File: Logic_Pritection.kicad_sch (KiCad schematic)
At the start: 18 parts

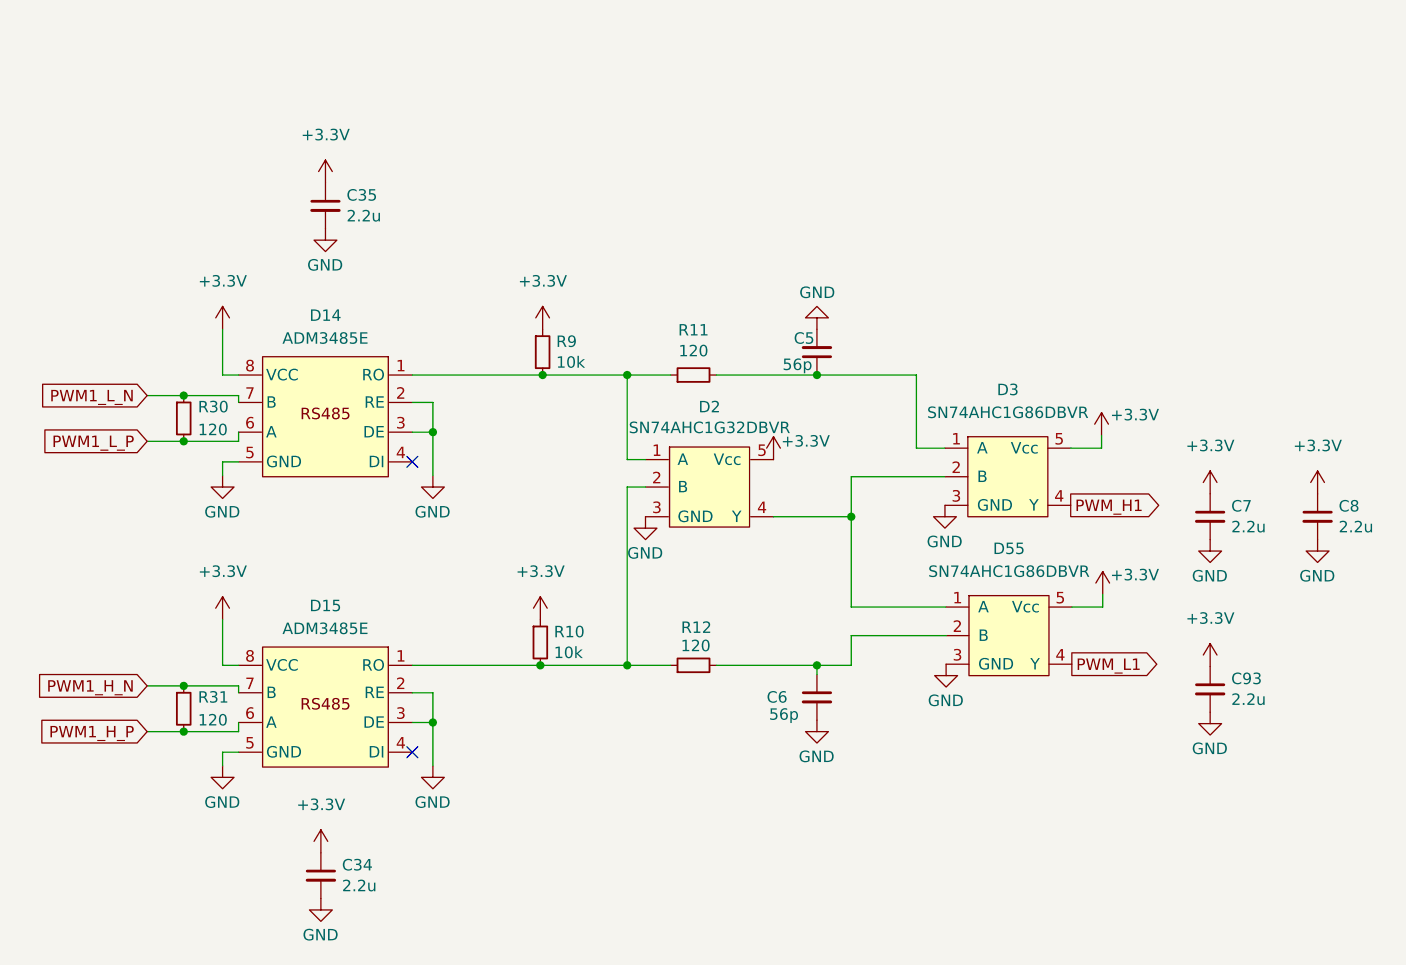
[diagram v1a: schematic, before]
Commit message: Изменил схему
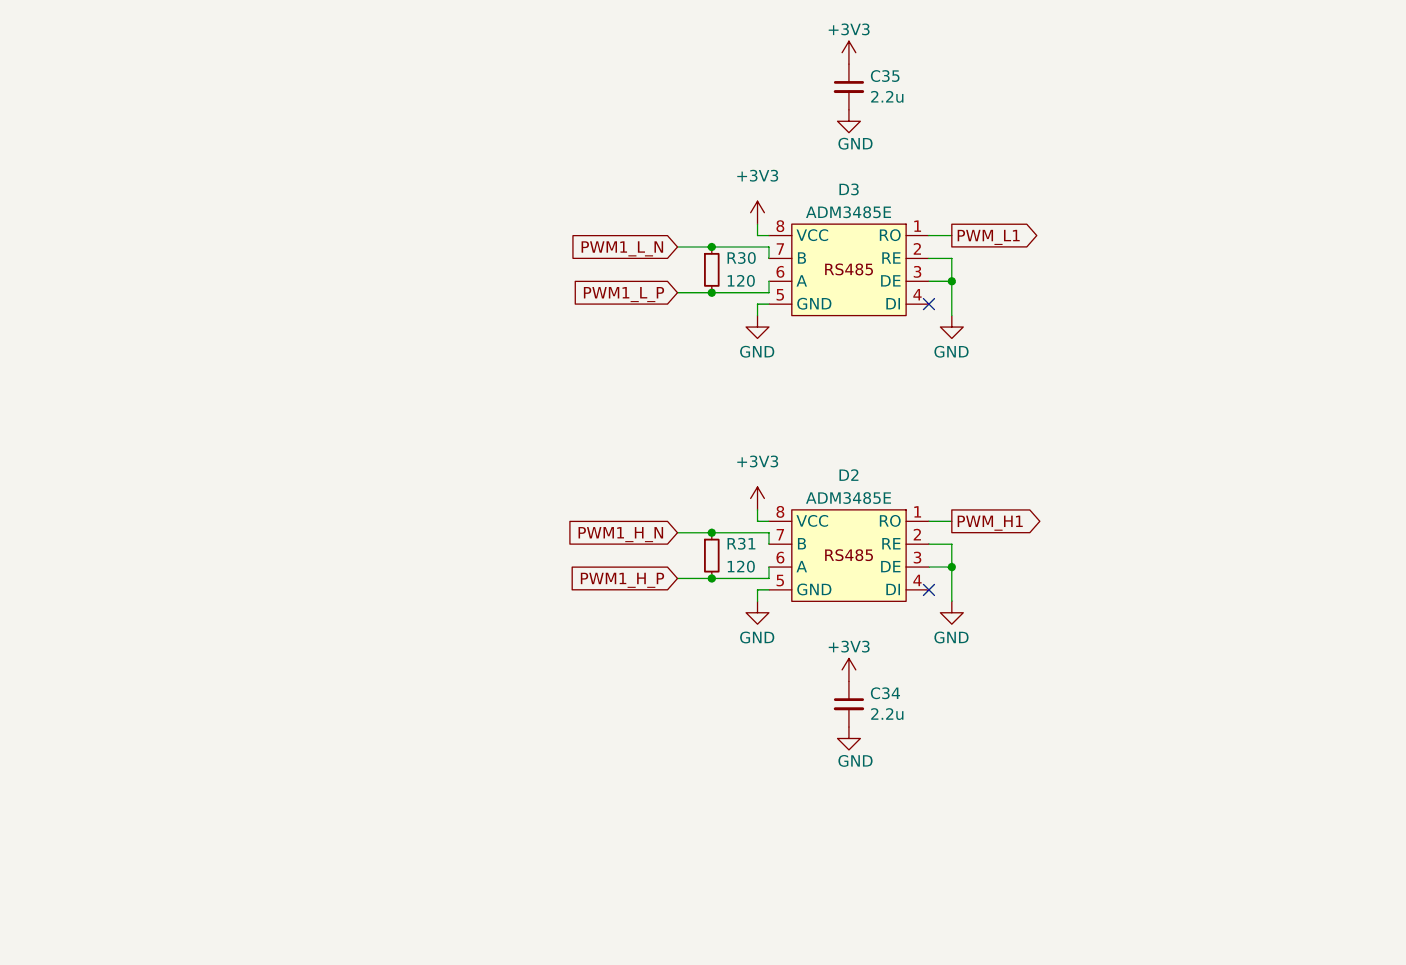
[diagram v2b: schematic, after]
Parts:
- removed C5, C6: 56p, Capacitor_SMD:C_0805_2012Metric_Pad1.18x1.45mm_HandSolder, symbol Device:C_Small
- removed C7, C8, C93: 2.2u, Capacitor_SMD:C_0805_2012Metric_Pad1.18x1.45mm_HandSolder, symbol Device:C_Small
- removed D14, D15: ADM3485E, Package_SO:SOIC-8_3.9x4.9mm_P1.27mm, symbol Interface_My:ADM3485E
- removed D2: SN74AHC1G32DBVR, Package_TO_SOT_SMD:SOT-23-5_HandSoldering, symbol Logic:SN74AHC1G86DBVR
- removed D3, D55: SN74AHC1G86DBVR, Package_TO_SOT_SMD:SOT-23-5_HandSoldering, symbol Logic:SN74AHC1G86DBVR
- removed R10, R9: 10k, Resistor_SMD:R_0805_2012Metric_Pad1.20x1.40mm_HandSolder, symbol Device:R_Small
- removed R11, R12: 120, Resistor_SMD:R_0805_2012Metric_Pad1.20x1.40mm_HandSolder, symbol Device:R_Small
- added D2, D3: ADM3485E, Package_SO:SOIC-8_3.9x4.9mm_P1.27mm, symbol Interface_My:ADM3485E_1
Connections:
- net +3V3: now also D2.8 (VCC), D3.8 (VCC)
- net GND: now also D2.2 (RE), D2.3 (DE), D2.5 (GND), D3.2 (RE), D3.3 (DE), D3.5 (GND)
- net PWM1_H_N: now also D2.7 (B)
- net PWM1_H_P: now also D2.6 (A)
- net PWM1_L_N: now also D3.7 (B)
- net PWM1_L_P: now also D3.6 (A)
- net PWM_H1: now also D2.1 (RO)
- net PWM_L1: now also D3.1 (RO)
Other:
- moved on the sheet: C34, C35, R30, R31

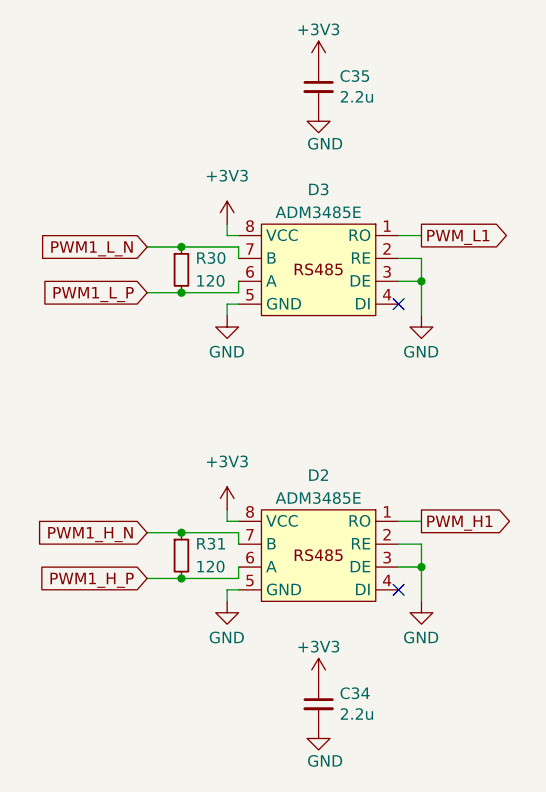
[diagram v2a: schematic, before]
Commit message: Убрал питание 3.3В
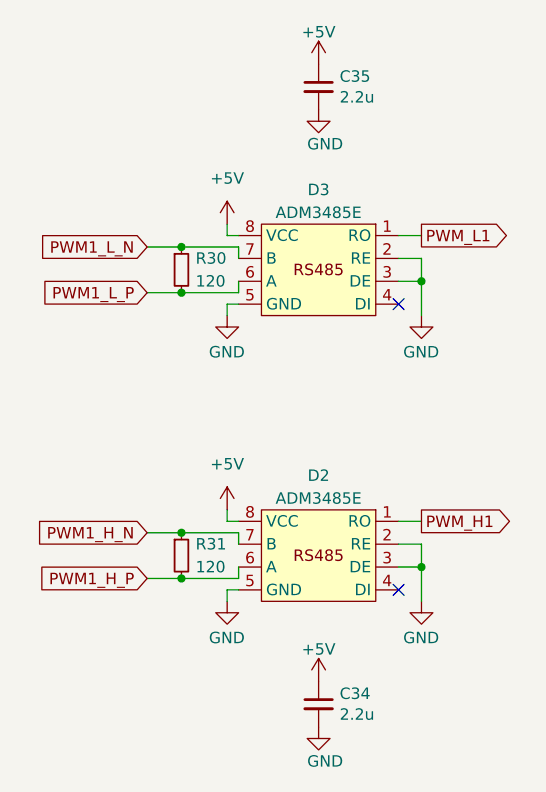
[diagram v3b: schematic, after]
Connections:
- net +3V3 renamed +5V
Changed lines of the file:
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@@
 	)
 	(symbol
-		(lib_id "power:+3.3V")
+		(lib_id "power:+5V")
 		(at 143.51 104.14 0)
 		(unit 1)
@@
 		(dnp no)
 		(fields_autoplaced yes)
-		(property "Reference" "#PWR012"
+		(property "Reference" "#PWR12"
 			(at 143.51 107.95 0)
 			(effects
@@
 			)
 		)
-		(property "Value" "+3V3"
-			(at 143.51 98.806 0)
+		(property "Value" "+5V"
+			(at 143.51 99.06 0)
 			(effects
 				(font
@@
 			)
 		)
-		(property "Description" ""
+		(property "Description" "Power symbol creates a global label with name \"+5V\""
 			(at 143.51 104.14 0)
 			(effects
@@
 			(project "Adapter"
 				(path "/e63e39d7-6ac0-4ffd-8aa3-1841a4541b55/7c11a07f-525c-45a7-9ad1-361ea90615cc"
-					(reference "#PWR012")
-					(unit 1)
-				)
-			)
-		)
-	)
-	(symbol
-		(lib_id "power:+3.3V")
+					(reference "#PWR12")
+					(unit 1)
+				)
+			)
+		)
+	)
+	(symbol
+		(lib_id "power:+5V")
 		(at 153.67 54.61 0)
 		(unit 1)
@@
 		(on_board yes)
 		(dnp no)
-		(property "Reference" "#PWR0147"
+		(property "Reference" "#PWR147"
 			(at 153.67 58.42 0)
 			(effects
@@
 			)
 		)
-		(property "Value" "+3V3"
-			(at 153.67 50.8 0)
+		(property "Value" "+5V"
+			(at 153.67 51.054 0)
 			(effects
 				(font
@@
 			)
 		)
-		(property "Description" ""
+		(property "Description" "Power symbol creates a global label with name \"+5V\""
 			(at 153.67 54.61 0)
 			(effects
@@
 			(project "Adapter"
 				(path "/e63e39d7-6ac0-4ffd-8aa3-1841a4541b55/7c11a07f-525c-45a7-9ad1-361ea90615cc"
-					(reference "#PWR0147")
+					(reference "#PWR147")
 					(unit 1)
 				)
@@
 	)
 	(symbol
-		(lib_id "power:+3.3V")
+		(lib_id "power:+5V")
 		(at 153.67 123.19 0)
 		(unit 1)
@@
 		(on_board yes)
 		(dnp no)
-		(property "Reference" "#PWR0145"
+		(property "Reference" "#PWR145"
 			(at 153.67 127 0)
 			(effects
@@
 			)
 		)
-		(property "Value" "+3V3"
-			(at 153.67 119.38 0)
+		(property "Value" "+5V"
+			(at 153.67 119.634 0)
 			(effects
 				(font
@@
 			)
 		)
-		(property "Description" ""
+		(property "Description" "Power symbol creates a global label with name \"+5V\""
 			(at 153.67 123.19 0)
 			(effects
@@
 			(project "Adapter"
 				(path "/e63e39d7-6ac0-4ffd-8aa3-1841a4541b55/7c11a07f-525c-45a7-9ad1-361ea90615cc"
-					(reference "#PWR0145")
+					(reference "#PWR145")
 					(unit 1)
 				)
@@
 	)
 	(symbol
-		(lib_id "power:+3.3V")
+		(lib_id "power:+5V")
 		(at 143.51 72.39 0)
 		(unit 1)
@@
 		(dnp no)
 		(fields_autoplaced yes)
-		(property "Reference" "#PWR010"
+		(property "Reference" "#PWR10"
 			(at 143.51 76.2 0)
 			(effects
@@
 			)
 		)
-		(property "Value" "+3V3"
-			(at 143.51 67.056 0)
+		(property "Value" "+5V"
+			(at 143.51 67.31 0)
 			(effects
 				(font
@@
 			)
 		)
-		(property "Description" ""
+		(property "Description" "Power symbol creates a global label with name \"+5V\""
 			(at 143.51 72.39 0)
 			(effects
@@
 			(project "Adapter"
 				(path "/e63e39d7-6ac0-4ffd-8aa3-1841a4541b55/7c11a07f-525c-45a7-9ad1-361ea90615cc"
-					(reference "#PWR010")
-					(unit 1)
-				)
+					(reference "#PWR10")
+					(unit 1)
+				)

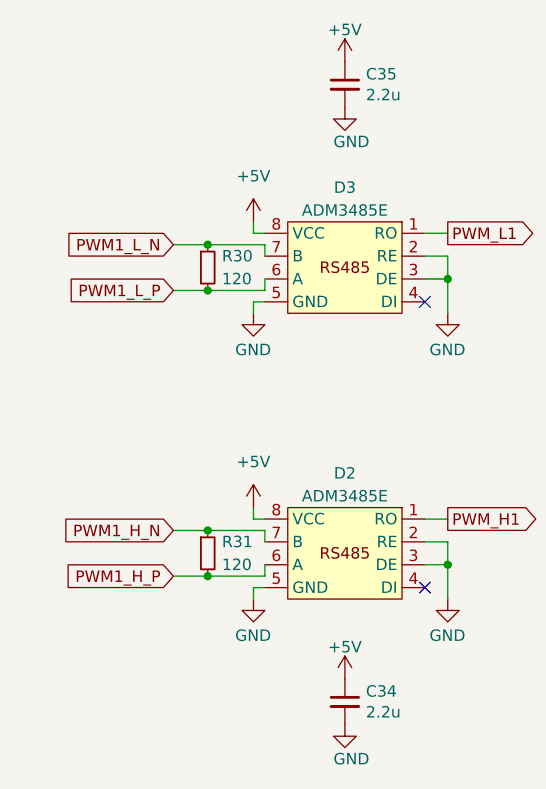
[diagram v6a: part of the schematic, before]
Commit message: Изменения: добавил подтяжки шины RS485
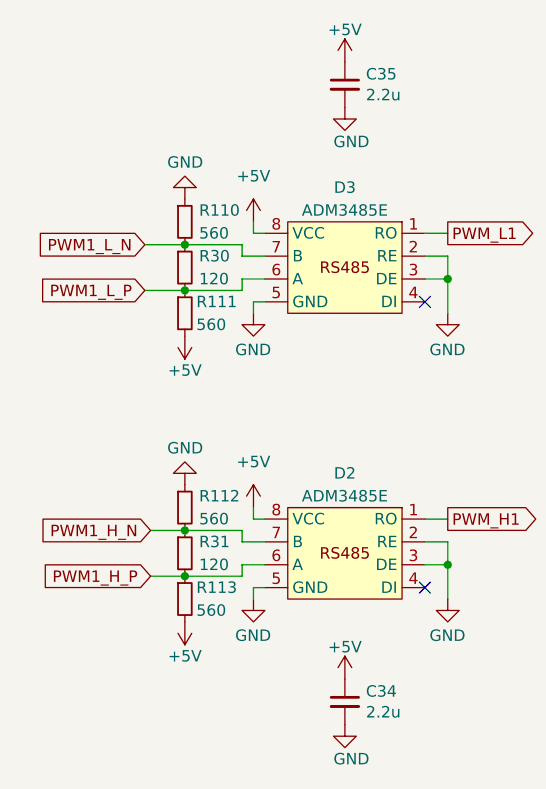
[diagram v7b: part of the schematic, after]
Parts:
- added R110, R111, R112, R113: 560, Resistor_SMD:R_0805_2012Metric_Pad1.20x1.40mm_HandSolder, symbol Device:R_Small
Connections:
- net +5V: now also R111.2, R113.2
- net GND: now also R110.1, R112.1
- net PWM1_H_N: now also R112.2
- net PWM1_H_P: now also R113.1
- net PWM1_L_N: now also R110.2
- net PWM1_L_P: now also R111.1
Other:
- moved on the sheet: R30, R31
